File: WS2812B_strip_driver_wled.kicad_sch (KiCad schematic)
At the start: 118 parts, among them J1 CH_1, J2 CH_2, J3 CH_3, J4 CH_4, J5 PWR_IN, J6 uPhone, J8 USB_C_Receptacle_USB2.0_16P, K1 RELAY_1, K2 RELAY_2, K3 RELAY_3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

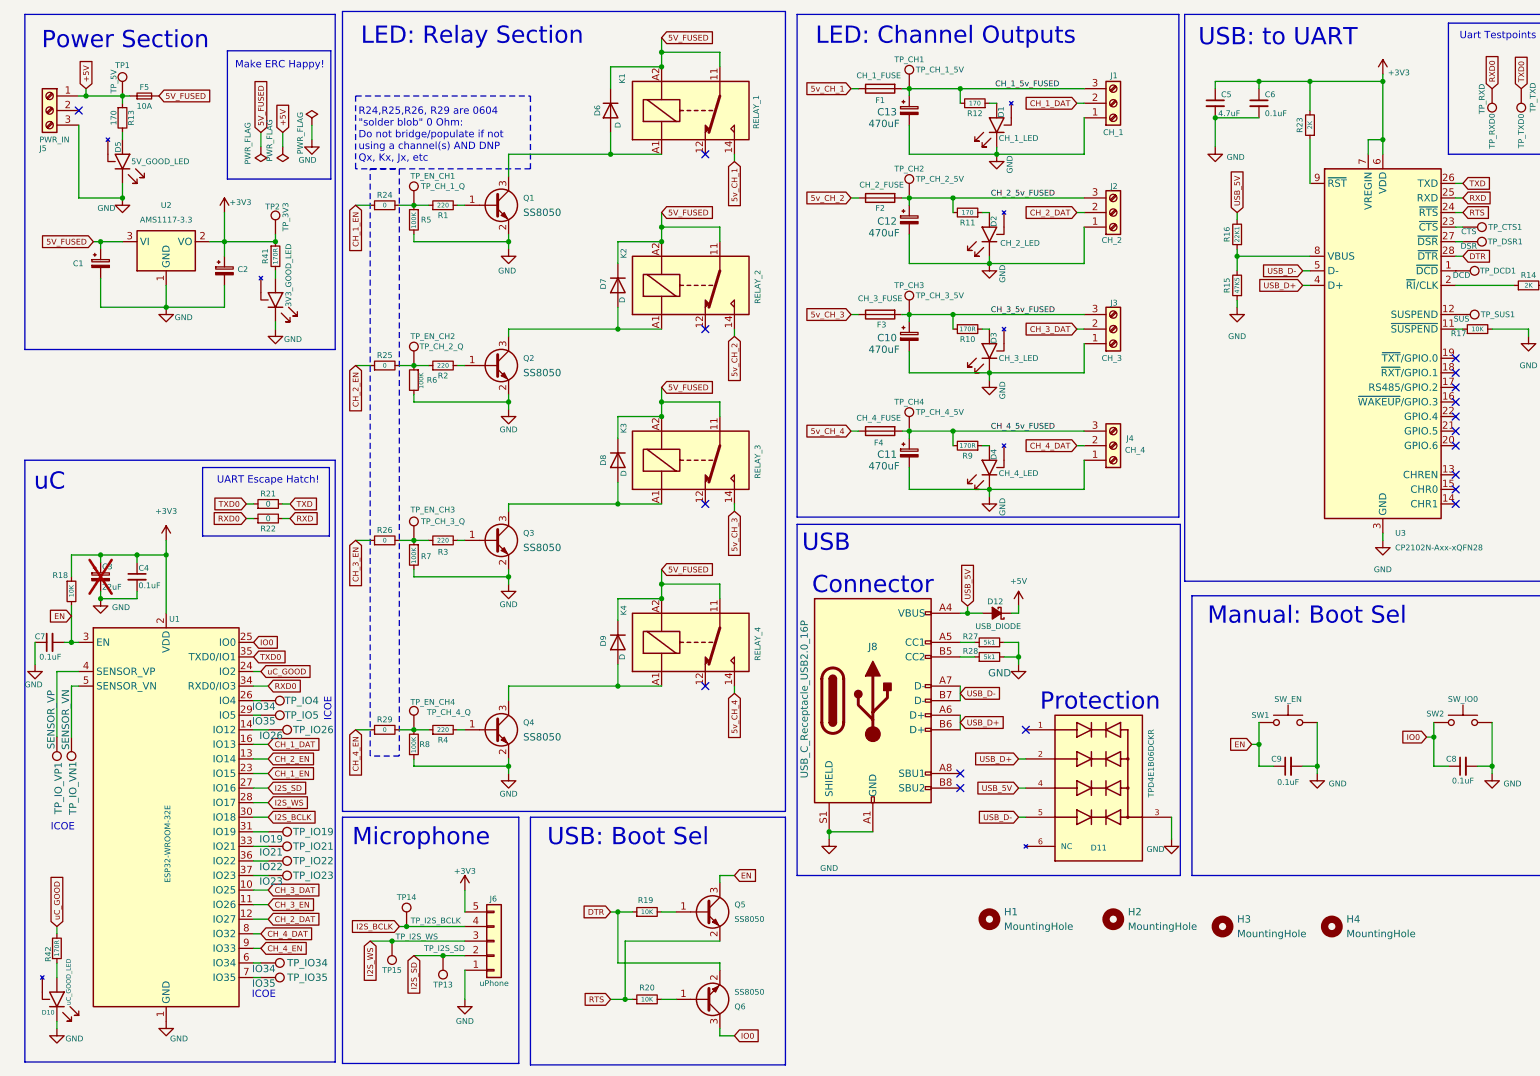
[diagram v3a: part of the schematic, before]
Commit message: swapped incorrect rx/tx pins
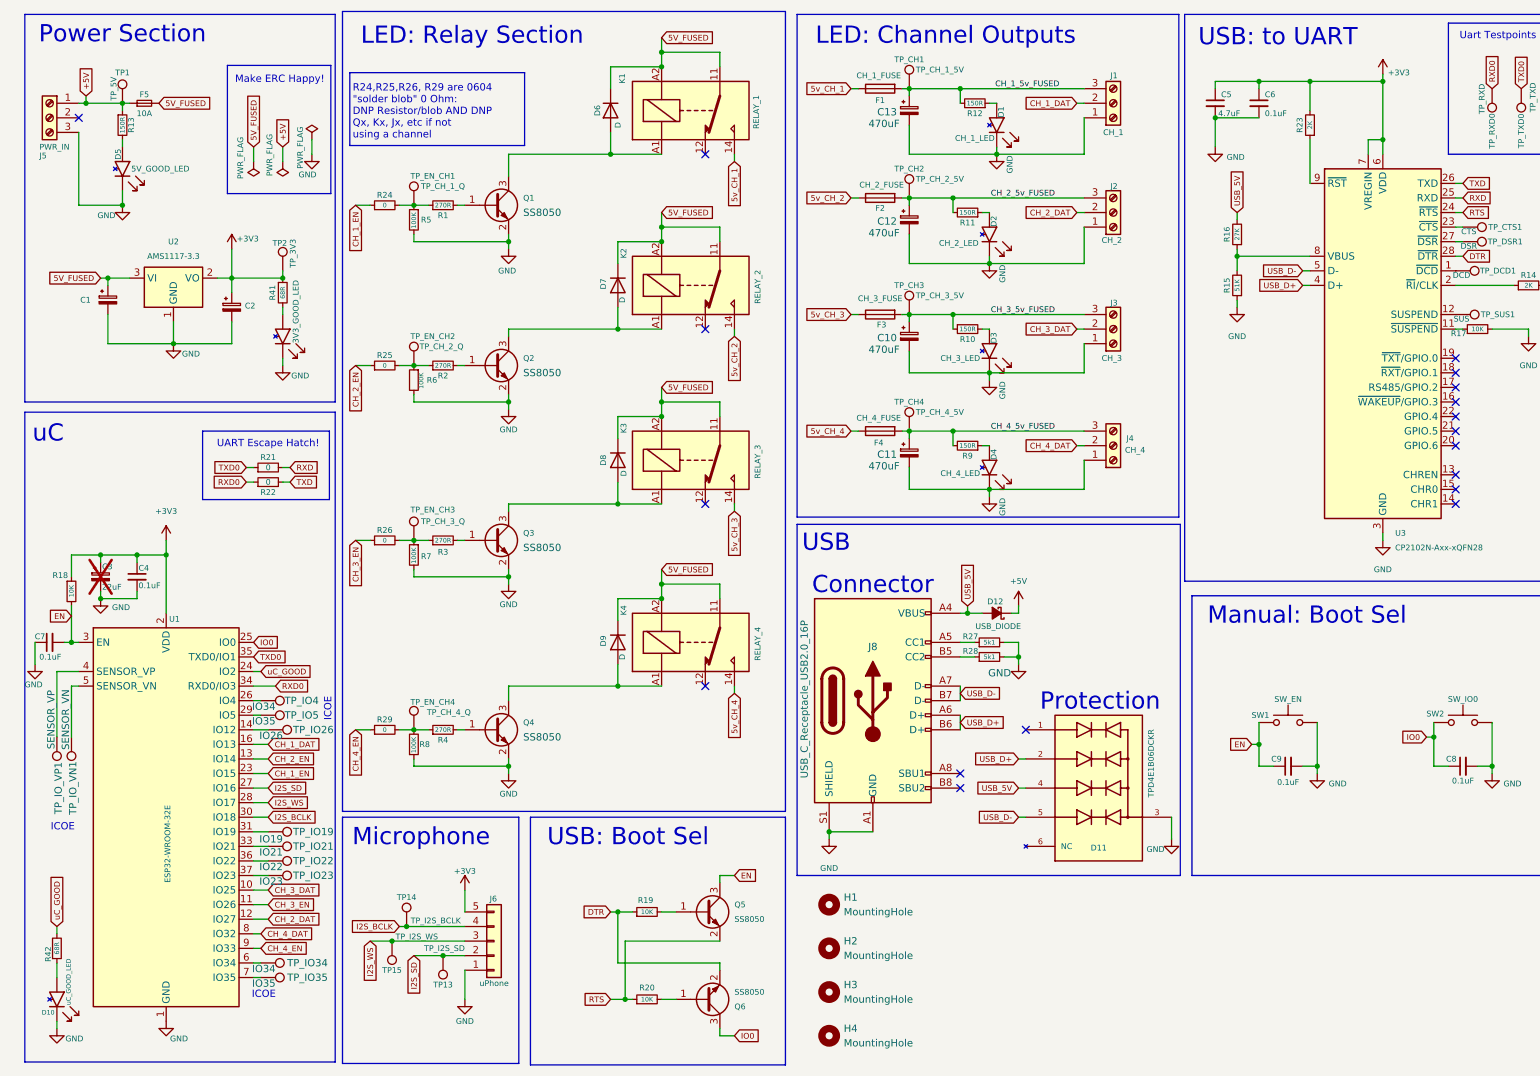
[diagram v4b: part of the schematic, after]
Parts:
- R1, R2, R3, R4: value 220 -> 270R
- R10, R9: value 170R -> 150R
- R11, R12, R13: value 170 -> 150R
- R15: value 47K5 -> 51K
- R16: value 22K1 -> 27K
- R41, R42: value 170R -> 68R
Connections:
- net RXD: now also R21.2; no longer R22.2
- net TXD: now also R22.2; no longer R21.2
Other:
- note added: "R24,R25,R26, R29 are 0604 "solder blob" 0 Ohm: DNP Resistor/blob AND DNP Qx, Kx, Jx, etc if not using a channel"
- note removed: "R24,R25,R26, R29 are 0604 "solder blob" 0 Ohm: Do not bridge/populate if not using a channel(s) AND DNP Qx, Kx, Jx, etc"
- moved on the sheet: C1, C2, F5, H1, H2, H3, H4, J5, R13, R21, R22, R41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

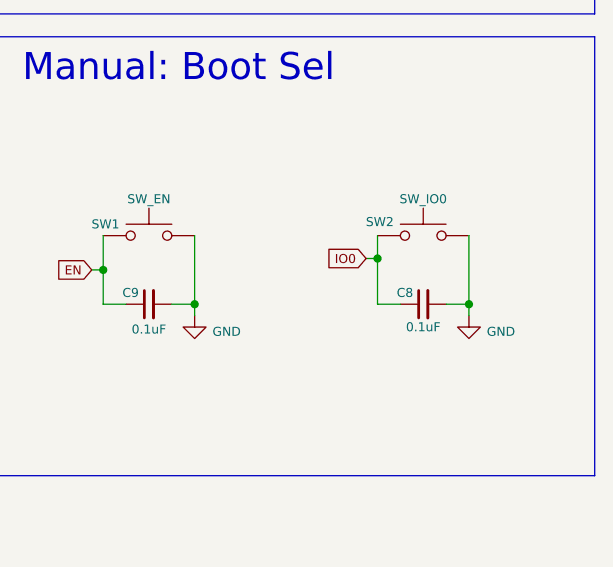
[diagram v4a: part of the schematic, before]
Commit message: swapped change en rc circuit vals, removed io btn debouncing cap. Board now fires straight up
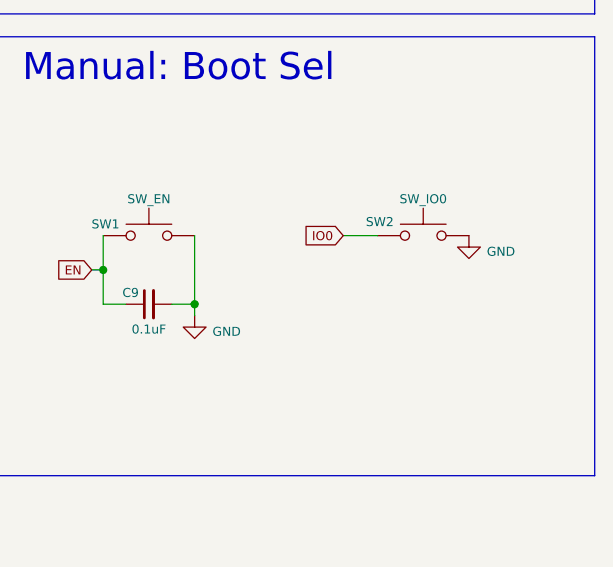
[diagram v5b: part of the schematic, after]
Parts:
- removed C8: 0.1uF, Capacitor_SMD:C_0805_2012Metric, symbol Device:C_Small
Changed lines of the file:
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@@
 	)
 	(junction
-		(at 269.24 144.78)
-		(diameter 0)
-		(color 0 0 0 0)
-	)
-	(junction
 		(at 181.61 96.52)
 		(diameter 0)
@@
 	)
 	(junction
-		(at 259.08 139.7)
-		(diameter 0)
-		(color 0 0 0 0)
-	)
-	(junction
 		(at 77.47 175.26)
 		(diameter 0)
@@
 	(wire
 		(pts
-			(xy 259.08 144.78) (xy 259.08 139.7)
-		)
-		(stroke
-			(width 0)
-			(type default)
-		)
-	)
-	(wire
-		(pts
 			(xy 97.79 113.03) (xy 97.79 111.76)
 		)
@@
 	(wire
 		(pts
-			(xy 257.81 139.7) (xy 259.08 139.7)
+			(xy 255.27 137.16) (xy 259.08 137.16)
 		)
 		(stroke
@@
 	(wire
 		(pts
-			(xy 269.24 146.05) (xy 269.24 144.78)
-		)
-		(stroke
-			(width 0)
-			(type default)
-		)
-	)
-	(wire
-		(pts
 			(xy 250.19 104.14) (xy 250.19 105.41)
 		)
@@
 	(wire
 		(pts
-			(xy 266.7 144.78) (xy 269.24 144.78)
-		)
-		(stroke
-			(width 0)
-			(type default)
-		)
-	)
-	(wire
-		(pts
 			(xy 53.34 176.53) (xy 54.61 176.53)
 		)
@@
 	(wire
 		(pts
-			(xy 269.24 137.16) (xy 269.24 144.78)
-		)
-		(stroke
-			(width 0)
-			(type default)
-		)
-	)
-	(wire
-		(pts
 			(xy 250.19 25.4) (xy 250.19 35.56)
 		)
@@
 	(wire
 		(pts
-			(xy 261.62 144.78) (xy 259.08 144.78)
-		)
-		(stroke
-			(width 0)
-			(type default)
-		)
-	)
-	(wire
-		(pts
 			(xy 124.46 81.28) (xy 124.46 83.82)
 		)
@@
 	(wire
 		(pts
-			(xy 259.08 137.16) (xy 259.08 139.7)
-		)
-		(stroke
-			(width 0)
-			(type default)
-		)
-	)
-	(wire
-		(pts
 			(xy 39.37 71.12) (xy 49.53 71.12)
 		)
@@
 	(global_label "IO0"
 		(shape input)
-		(at 257.81 139.7 180)
+		(at 255.27 137.16 180)
 		(fields_autoplaced yes)
 		(effects
@@
 		)
 		(property "Intersheetrefs" "${INTERSHEET_REFS}"
-			(at 252.9835 139.7 0)
+			(at 250.4435 137.16 0)
 			(effects
 				(font
@@
 	)
 	(symbol
-		(lib_id "Device:C_Small")
-		(at 264.16 144.78 90)
-		(unit 1)
-		(exclude_from_sim no)
-		(in_bom yes)
-		(on_board yes)
-		(dnp no)
-		(property "Reference" "C8"
-			(at 262.128 143.51 90)
-			(effects
-				(font
-					(size 1 1)
-				)
-			)
-		)
-		(property "Value" "0.1uF"
-			(at 264.16 147.32 90)
-			(effects
-				(font
-					(size 1 1)
-				)
-			)
-		)
-		(property "Footprint" "Capacitor_SMD:C_0805_2012Metric"
-			(at 264.16 144.78 0)
-			(effects
-				(font
-					(size 1 1)
-				)
-				(hide yes)
-			)
-		)
-		(property "Datasheet" "~"
-			(at 264.16 144.78 0)
-			(effects
-				(font
-					(size 1 1)
-				)
-				(hide yes)
-			)
-		)
-		(property "Description" "Unpolarized capacitor, small symbol"
-			(at 264.16 144.78 0)
-			(effects
-				(font
-					(size 1 1)
-				)
-				(hide yes)
-			)
-		)
-		(pin "1"
-		)
-		(pin "2"
-		)
-		(instances
-			(project ""
-				(path "/a67e84d5-b812-4302-b0a6-200741099847"
-					(reference "C8")
-					(unit 1)
-				)
-			)
-		)
-	)
-	(symbol
 		(lib_id "Relay:JQC-3FF-005-1Z")
 		(at 129.54 123.19 0)
@@
 	(symbol
 		(lib_id "power:GND")
-		(at 269.24 146.05 0)
+		(at 269.24 137.16 0)
 		(unit 1)
 		(exclude_from_sim no)
@@
 		(dnp no)
 		(property "Reference" "#PWR035"
-			(at 269.24 152.4 0)
+			(at 269.24 143.51 0)
 			(effects
 				(font
@@
 		)
 		(property "Value" "GND"
-			(at 272.796 147.828 0)
+			(at 272.796 138.938 0)
 			(effects
 				(font
@@
 		)
 		(property "Footprint" ""
-			(at 269.24 146.05 0)
+			(at 269.24 137.16 0)
 			(effects
 				(font
@@
 		)
 		(property "Datasheet" ""
-			(at 269.24 146.05 0)
+			(at 269.24 137.16 0)
 			(effects
 				(font
@@
 		)
 		(property "Description" "Power symbol creates a global label with name \"GND\" , ground"
-			(at 269.24 146.05 0)
+			(at 269.24 137.16 0)
 			(effects
 				(font

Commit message: swapped change en rc circuit vals, removed io btn debouncing cap. Board now fires straight up
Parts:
- C7: value 0.1uF -> 1uF
- R18: value 10K -> 51K
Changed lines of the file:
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@@
 			)
 		)
-		(property "Value" "0.1uF"
+		(property "Value" "1uF"
 			(at 19.812 125.73 90)
 			(effects
@@
 			)
 		)
-		(property "Value" "10K"
+		(property "Value" "51K"
 			(at 21.59 115.316 90)
 			(effects
